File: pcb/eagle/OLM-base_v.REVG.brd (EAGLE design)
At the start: 92.1 x 57.6 mm, 40 parts, among them IC1 ATMEGA, IC2 MCP1702-33, IC3 ENC28J60SP, IC4 DS1307, J1 POWER_JACKPTH, J2 MAGJACK, U1 USD-SOCKETMICRO-SD-SOCKET-TAO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, X1 16 MHz, X2 25MHz, X3 32.657k

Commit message: made changes
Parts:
- removed JP1: BATT, SparkFun:1X02_LOCK_LONGPADS
- removed JP2: (no value), SparkFun-Connectors:1X08_LOCK
- added CN1: (no value), adafruit:JST-PH-2-THM-RA
- added JP4: M10LOCK, SparkFun-Connectors:1X10_LOCK
- moved RN1 27.0 mm to (48.8, 13.5), turned to 90 degrees
- moved X3 22.4 mm to (52.8, 35.3), turned to 180 degrees
- moved X2 20.2 mm to (64.5, 49.3), turned to 180 degrees
- moved J1 7.77 mm to (0.25, 15.2)
- moved JP3 5.34 mm to (6.86, 55.9)
- moved C8 4.93 mm to (24.4, 38.1), turned to 90 degrees
- moved L1 3.39 mm to (8.13, 42.7)
- moved C7 3.21 mm to (28.2, 38.1), turned to 90 degrees
- moved CX1 3.18 mm to (32.3, 45.7)
- moved J2 3.10 mm to (0.51, 38.1)
- moved SV1 3.07 mm to (6.60, 50.0), turned to 180 degrees
- moved IC4 2.75 mm to (48.5, 45.7)
- moved CX2 2.55 mm to (32.5, 41.7)
- moved FTDI 2.30 mm to (70.9, 55.9)
- moved R5 2.05 mm to (17.5, 47.5)
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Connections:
- net A4/SDA: now also JP4.10; no longer JP2.8
- net A5/SCL: now also JP4.9; no longer JP2.7
- net D2: now also JP4.3; no longer JP2.4
- net D3/PWM: now also JP4.2; no longer JP2.3
- net D4: now also JP4.6
- net D6/PWM: now also JP4.5
- net D7: now also JP4.4
- net E-CLK: now also JP4.8; no longer JP2.6
- net E-INT: now also JP4.7; no longer JP2.5
- net GND: now also CN1.2, JP4.1; no longer JP1.2, JP2.1
- net MISO/D12: now also U1.7
- net MOSI/D11: now also U1.3
- net SCK/D13: now also U1.5
- net VCC: now also JP3.8; no longer JP2.2
- net VIN: now also CN1.1; no longer JP1.1, JP3.8
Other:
- board text added: "+"
- board text added: "X1"

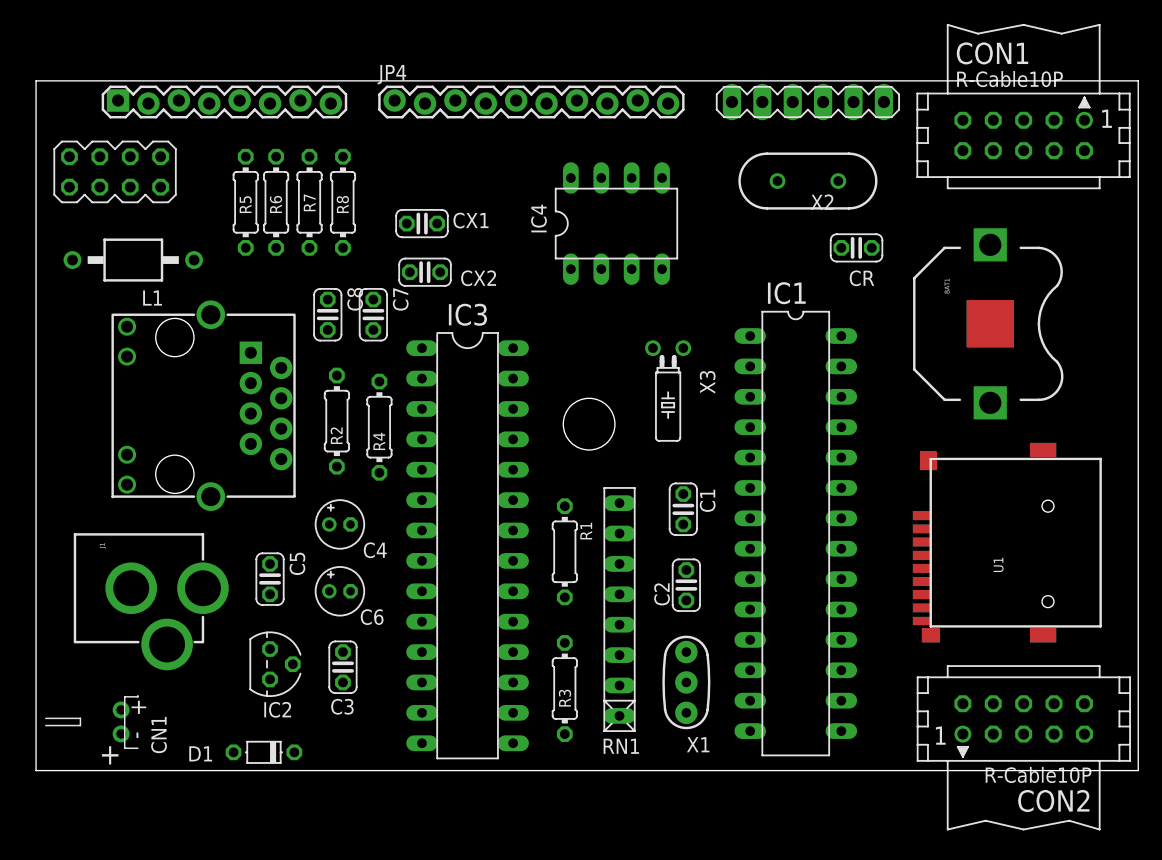
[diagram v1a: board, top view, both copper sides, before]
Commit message: rewired OLM-base-REVG
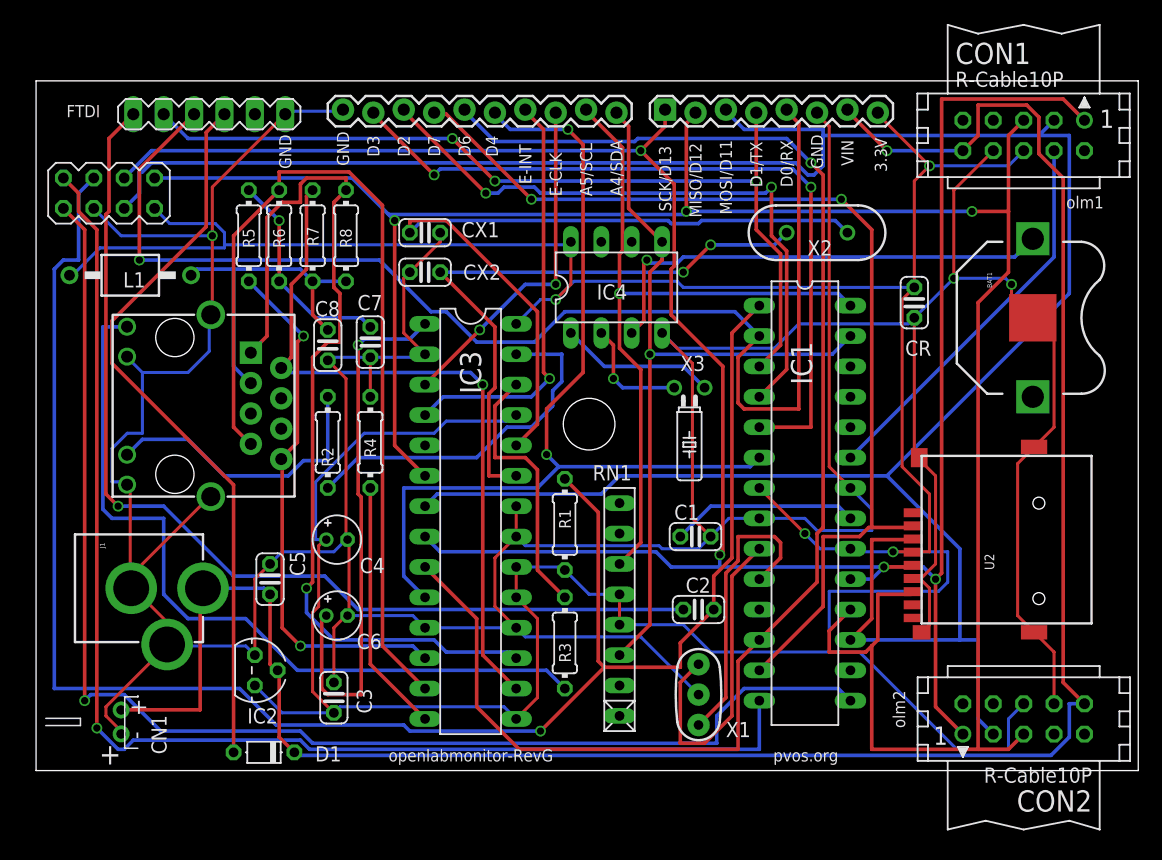
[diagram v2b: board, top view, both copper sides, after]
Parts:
- removed U1: USD-SOCKETMICRO-SD-SOCKET-TAOBAO, SparkFunNew:MICRO-SD-SOCKET-TAOBAO
- added U2: USD-SOCKETMICRO-SD-SOCKET-TAOBAO, SparkFunNew:MICRO-SD-SOCKET-TAOBAO
- moved FTDI 50.0 mm to (20.8, 54.9)
- moved JP3 45.7 mm to (52.6, 55.1)
- moved CR 6.65 mm to (73.4, 39.1), turned to 270 degrees
- moved IC4 5.33 mm to (48.5, 40.4)
- moved X2 4.38 mm to (65.3, 45.0)
- moved JP4 4.38 mm to (25.7, 55.1)
- moved R3 3.81 mm to (44.2, 10.7)
- moved X3 3.75 mm to (54.6, 32.0)
- moved BAT1 3.59 mm to (83.3, 37.8)
- moved R5 2.81 mm to (17.8, 44.7)
- moved R6 2.81 mm to (20.3, 44.7)
- moved R7 2.81 mm to (23.1, 44.7)
- moved R8 2.81 mm to (25.9, 44.7)
- moved C3 2.65 mm to (24.9, 6.10)
- moved IC1 2.65 mm to (64.3, 22.4)
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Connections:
- net D7: now also U2.2; no longer U1.2
- net GND: now also U2.6, U2.GND1, U2.GND3, U2.P$1, U2.P$2; no longer U1.6, U1.GND1, U1.GND3, U1.P$1, U1.P$2
- net MISO/D12: now also U2.7; no longer U1.7
- net MOSI/D11: now also U2.3; no longer U1.3
- net SCK/D13: now also U2.5; no longer U1.5
- net VCC: now also U2.4; no longer U1.4
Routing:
- net GND: track 0.00 -> 413.6 mm, vias 0 -> 3
- net VCC: track 0.00 -> 310.3 mm, vias 0 -> 4
- net MOSI/D11: track 0.00 -> 218.4 mm
- net SCK/D13: track 0.00 -> 203.1 mm, vias 0 -> 4
- net MISO/D12: track 0.00 -> 196.1 mm, vias 0 -> 3
- net VIN: track 0.00 -> 178.2 mm, vias 0 -> 1
- net RESET: track 0.00 -> 150.9 mm, vias 0 -> 1
- net D6/PWM: track 0.00 -> 120.3 mm, vias 0 -> 1
- net PB1/D9/PWM: track 0.00 -> 111.4 mm, vias 0 -> 1
- net PB0/D8: track 0.00 -> 107.9 mm, vias 0 -> 1
- net D0/RX: track 0.00 -> 107.7 mm, vias 0 -> 1
- net D7: track 0.00 -> 86.9 mm, vias 0 -> 2
- net N$20: track 0.00 -> 85.0 mm, vias 0 -> 1
- net TD+: track 0.00 -> 78.5 mm, vias 0 -> 1
- net D4: track 0.00 -> 77.8 mm, vias 0 -> 2
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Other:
- board text added: "3.3V"
- board text added: "A4/SDA"
- board text added: "A5/SCL"
- board text added: "D0/RX"
- board text added: "D1/TX"
- board text added: "D2"
- board text added: "D3"
- board text added: "D4"
- board text added: "D6"
- board text added: "D7"
- board text added: "E-CLK"
- board text added: "E-INT"
- board text added: "FTDI"
- board text added: "GND"
- board text added: "MISO/D12"
- board text added: "MOSI/D11"
- board text added: "SCK/D13"
- board text added: "VIN"
- board text added: "olm1"
- board text added: "olm2"
- board text added: "openlabmonitor-RevG"
- board text added: "pvos.org"

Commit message: fixed breakouts by adding reset pin
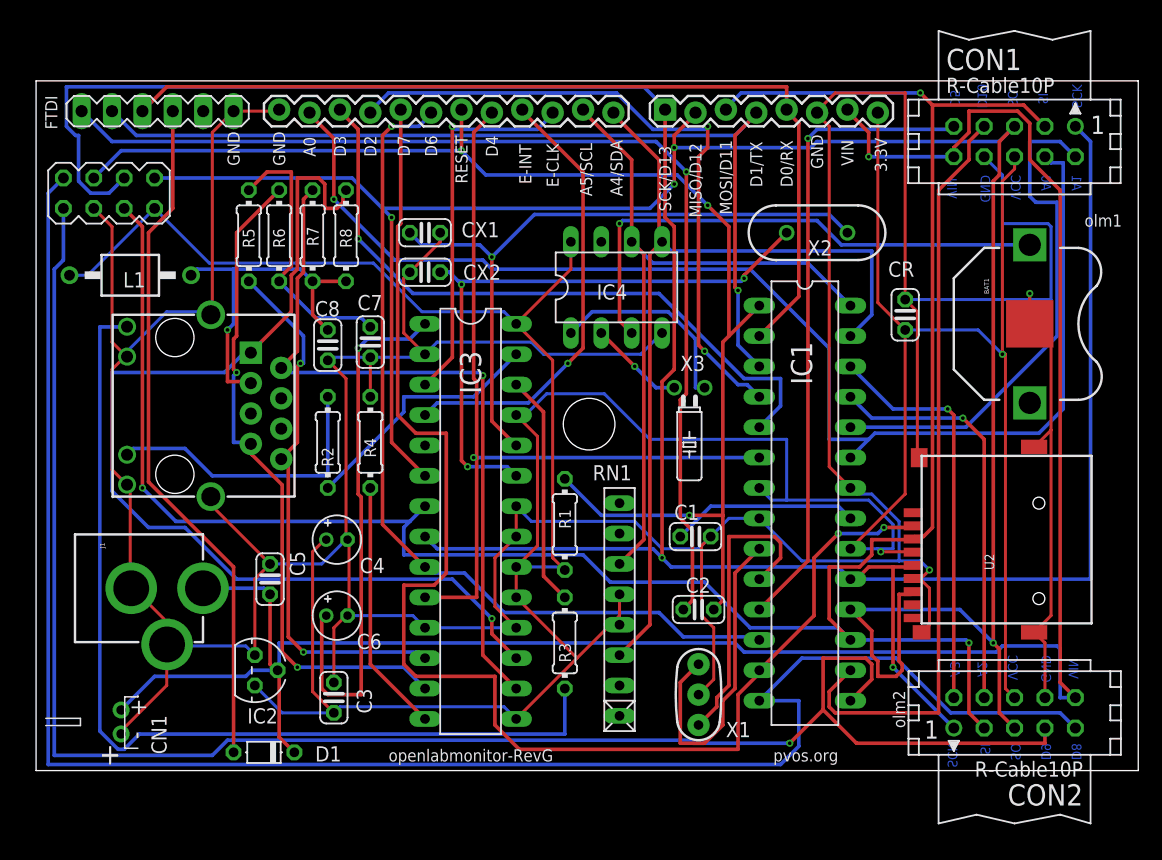
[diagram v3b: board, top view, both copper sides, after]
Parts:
- removed JP4: M10LOCK, SparkFun-Connectors:1X10_LOCK
- added JP1: M12LOCK, SparkFun-Connectors:1X12_LOCK
- moved FTDI 4.33 mm to (16.5, 55.1)
- moved CR 1.27 mm to (72.6, 38.1), turned to 90 degrees
- moved CON2 0.92 mm to (81.8, 4.83)
- moved CON1 0.92 mm to (81.8, 52.6)
- moved BAT1 0.57 mm to (83.1, 37.3)
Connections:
- net A0: now also JP1.2
- net A1: now also CON1.2
- net A2: now also CON2.4
- net A3: now also CON2.2
- net A4/SDA: now also JP1.12; no longer JP4.10
- net A5/SCL: now also JP1.11; no longer JP4.9
- net D10/PWM: now also CON1.7
- net D2: now also JP1.4; no longer JP4.3
- net D3/PWM: now also JP1.3; no longer JP4.2
- net D4: now also JP1.8; no longer JP4.6
- net D5/PWM: now also CON1.9
- net D6/PWM: now also JP1.6; no longer JP4.5
- net D7: now also JP1.5; no longer JP4.4
- net E-CLK: now also JP1.10; no longer JP4.8
- net E-INT: now also JP1.9; no longer JP4.7
- net GND: now also JP1.1; no longer JP4.1
- net PB0/D8: now also CON2.9
- net PB1/D9/PWM: now also CON2.7
- net RESET: now also JP1.7
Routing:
- net A0: track 32.9 -> 107.3 mm, vias 0 -> 1
- net D10/PWM: track 0.00 -> 63.7 mm
- net D5/PWM: track 0.00 -> 53.7 mm, vias 0 -> 1
- net D6/PWM: track 120.3 -> 72.9 mm
- net A1: track 0.00 -> 43.0 mm
- net PB0/D8: track 107.9 -> 150.3 mm, vias 1 -> 0
- net RESET: track 150.9 -> 110.7 mm, vias 1 -> 3
- net A2: track 0.00 -> 34.2 mm, vias 0 -> 1
- net PB1/D9/PWM: track 111.4 -> 145.4 mm
- net A3: track 0.00 -> 33.9 mm, vias 0 -> 1
- net D0/RX: track 107.7 -> 77.3 mm, vias 1 -> 0
- net D7: track 86.9 -> 113.9 mm
- net MOSI/D11: track 218.4 -> 191.6 mm, vias 0 -> 3
- net RD+: track 76.6 -> 56.0 mm, vias 0 -> 2
- net SCK/D13: track 203.1 -> 219.1 mm, vias 4 -> 2
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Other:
- board text added: "A0"
- board text added: "A1"
- board text added: "A2"
- board text added: "A3"
- board text added: "D10"
- board text added: "D5"
- board text added: "D8"
- board text added: "D9"
- board text added: "RESET"
- board text added: "SCK"
- board text added: "SI"
- board text added: "SO"
- board text added: "VCC"

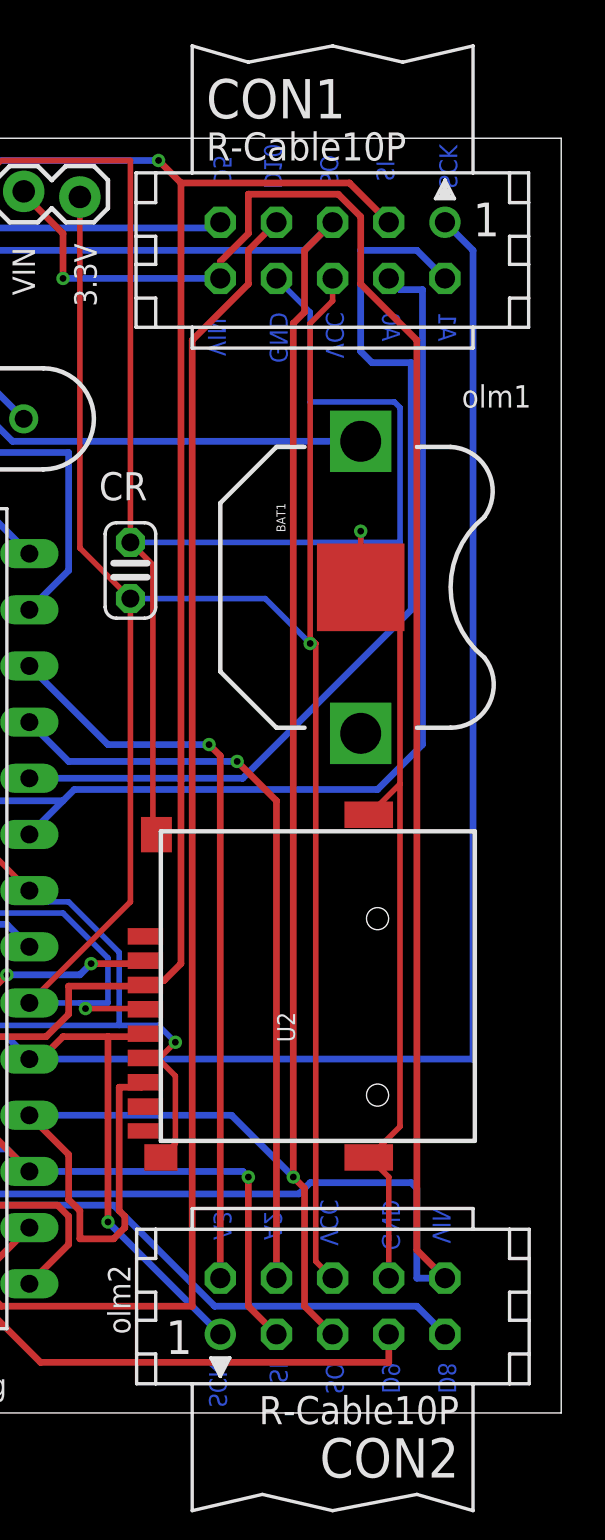
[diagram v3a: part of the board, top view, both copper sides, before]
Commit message: removed pin labels on bottom of board to satisfy seeed design rules
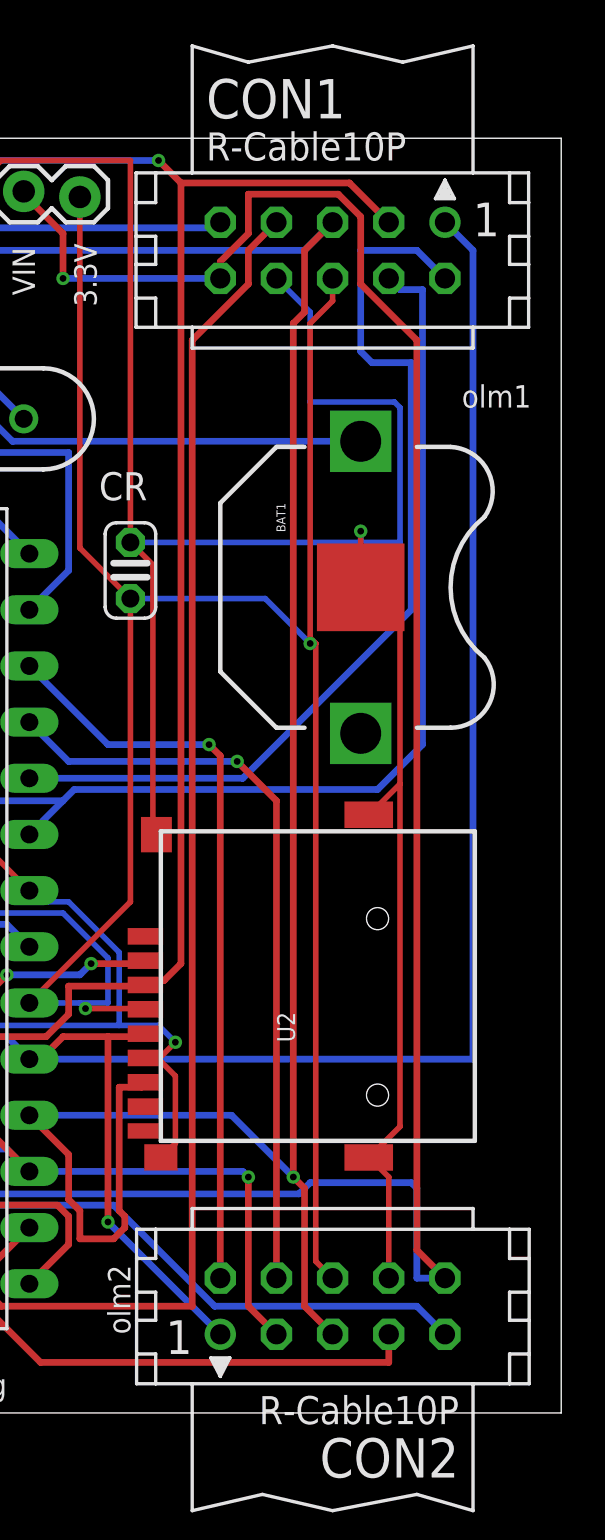
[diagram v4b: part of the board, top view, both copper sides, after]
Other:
- board text removed: "A1"
- board text removed: "A2"
- board text removed: "A3"
- board text removed: "D10"
- board text removed: "D5"
- board text removed: "D8"
- board text removed: "D9"
- board text removed: "SCK"
- board text removed: "SI"
- board text removed: "SO"
- board text removed: "VCC"
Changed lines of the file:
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@@
 <text x="35.052" y="53.086" size="1.016" layer="21" rot="R270">RESET</text>
 <text x="23.368" y="51.308" size="1.016" layer="21" rot="R90">A0</text>
-<text x="87.122" y="9.398" size="0.8128" layer="16" rot="MR270">VIN</text>
-<text x="84.836" y="9.652" size="0.8128" layer="16" rot="MR270">GND</text>
-<text x="82.042" y="9.652" size="0.8128" layer="16" rot="MR270">VCC</text>
-<text x="79.502" y="9.144" size="0.8128" layer="16" rot="MR270">A2</text>
-<text x="77.216" y="9.144" size="0.8128" layer="16" rot="MR270">A3</text>
-<text x="87.376" y="2.286" size="0.8128" layer="16" rot="MR270">D8</text>
-<text x="84.836" y="2.286" size="0.8128" layer="16" rot="MR270">D9</text>
-<text x="82.296" y="2.286" size="0.8128" layer="16" rot="MR270">SO</text>
-<text x="79.756" y="2.286" size="0.8128" layer="16" rot="MR270">SI</text>
-<text x="76.2" y="0.254" size="0.8128" layer="16" rot="MR90">SCK</text>
-<text x="77.216" y="56.896" size="0.8128" layer="16" rot="MR270">D5</text>
-<text x="79.502" y="57.404" size="0.8128" layer="16" rot="MR270">D10</text>
-<text x="82.042" y="56.896" size="0.8128" layer="16" rot="MR270">SO</text>
-<text x="84.582" y="56.642" size="0.8128" layer="16" rot="MR270">SI</text>
-<text x="86.614" y="55.372" size="0.8128" layer="16" rot="MR90">SCK</text>
-<text x="76.962" y="49.53" size="0.8128" layer="16" rot="MR270">VIN</text>
-<text x="79.756" y="49.784" size="0.8128" layer="16" rot="MR270">GND</text>
-<text x="82.296" y="49.784" size="0.8128" layer="16" rot="MR270">VCC</text>
-<text x="84.836" y="49.784" size="0.8128" layer="16" rot="MR270">A0</text>
-<text x="87.376" y="49.784" size="0.8128" layer="16" rot="MR270">A1</text>
 </plain>
 <attributes>
